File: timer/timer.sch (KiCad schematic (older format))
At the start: 29 parts, among them P1 Keypad, P2 Display, P3 Handset, P4 PWR, P5 Hook, P6 Encoder, P7 SPKR, Q1 S8050, U1 74HC595, U2 NanoEvery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

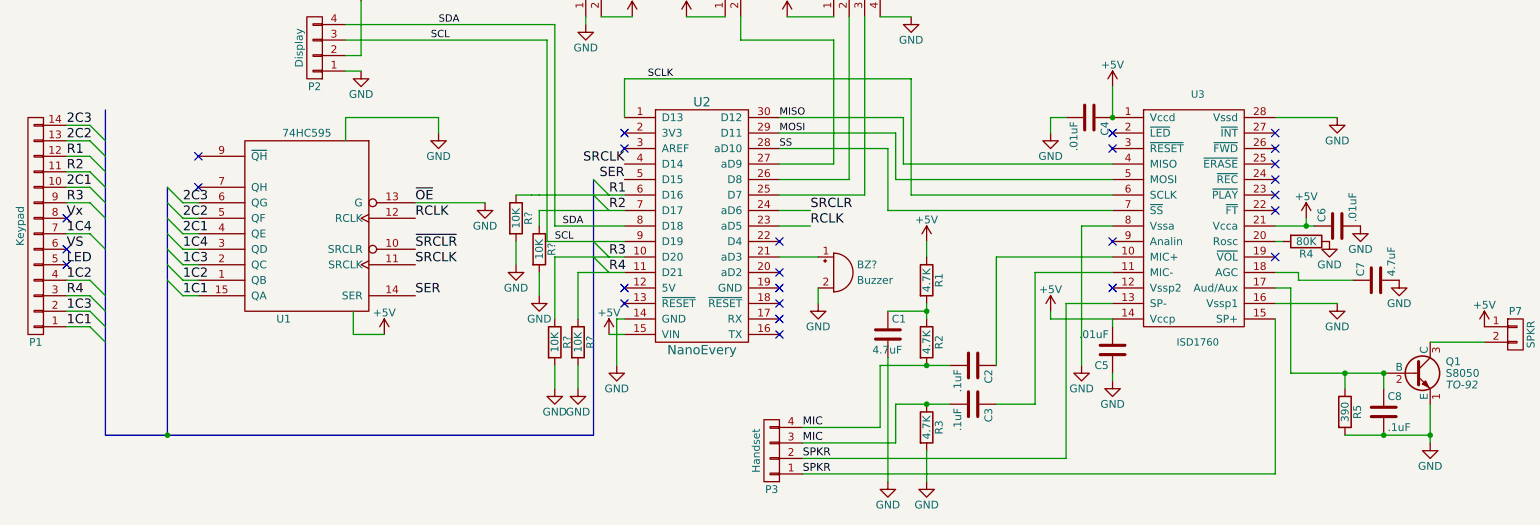
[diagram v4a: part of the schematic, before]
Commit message: More moved buzzer t d2
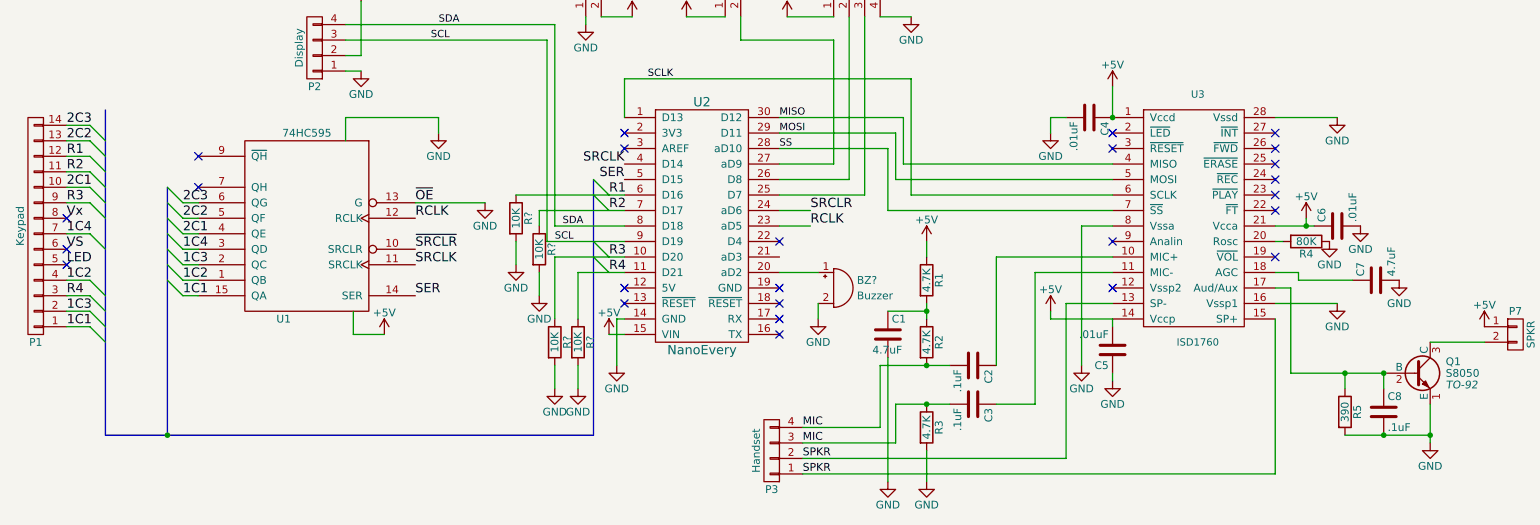
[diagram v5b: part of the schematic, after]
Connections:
- net at U2.20 (aD2): now also BZ?.1 (-)
- net at U2.21 (aD3): no longer BZ?.1 (-)
- no-connect marks 26 -> 25
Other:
- moved on the sheet: BZ?
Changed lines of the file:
@@
 	3050 2400 3050 2050
 Wire Wire Line
-	4250 3600 4550 3600
-Wire Wire Line
-	4550 3600 4750 3600
+	4250 3600 4750 3600
 Wire Wire Line
 	4250 3600 4250 2300
@@
 	7500 2800 7500 2900
 Wire Wire Line
-	8950 3500 9150 3500
-Wire Wire Line
-	9150 3500 9200 3500
+	8950 3500 9200 3500
 Wire Wire Line
 	8950 3800 9100 3800
@@
 	7150 3700 7900 3700
 Wire Wire Line
-	6700 4000 6700 4050
-Wire Wire Line
-	6700 4050 6700 4100
+	6700 4000 6700 4100
 Wire Wire Line
 	6700 4950 6700 5150
@@
 	6400 4800 6400 4400
 Wire Wire Line
-	6400 4400 6700 4400
-Wire Wire Line
-	6700 4400 6850 4400
+	6400 4400 6850 4400
 Wire Wire Line
 	5900 4900 6500 4900
@@
 	6500 4900 6500 4650
 Wire Wire Line
-	6500 4650 6700 4650
-Wire Wire Line
-	6700 4650 6850 4650
+	6500 4650 6850 4650
 Connection ~ 6700 4650
 Connection ~ 6700 4050
@@
 	9050 3900 9050 4450
 Wire Wire Line
-	9050 4450 9400 4450
-Wire Wire Line
-	9400 4450 9650 4450
+	9050 4450 9650 4450
 Connection ~ 9400 4450
 Connection ~ 9650 4450
@@
 	9650 4450 9650 4550
 Wire Wire Line
-	9400 4850 9650 4850
-Wire Wire Line
-	9650 4850 9950 4850
-Wire Wire Line
-	9950 4650 9950 4850
-Wire Wire Line
-	9950 4850 9950 4900
+	9400 4850 9950 4850
+Wire Wire Line
+	9950 4650 9950 4900
 Connection ~ 9950 4850
 Connection ~ 9650 4850
@@
 	3400 3350 3850 3350
 Wire Bus Line
-	1400 2750 1400 2950
+	1400 2750 1400 4850
 Wire Bus Line
-	1400 2950 1400 3050
-Wire Bus Line
-	1400 3050 1400 3150
-Wire Bus Line
-	1400 3150 1400 3250
-Wire Bus Line
-	1400 3250 1400 3350
-Wire Bus Line
-	1400 3350 1400 3450
-Wire Bus Line
-	1400 3450 1400 3650
-Wire Bus Line
-	1400 3650 1400 3950
-Wire Bus Line
-	1400 3950 1400 4050
-Wire Bus Line
-	1400 4050 1400 4150
-Wire Bus Line
-	1400 4150 1400 4250
-Wire Bus Line
-	1400 4250 1400 4850
-Wire Bus Line
-	4550 4850 4550 3700
-Wire Bus Line
-	4550 3700 4550 3600
-Wire Bus Line
-	4550 3600 4550 3300
-Wire Bus Line
-	4550 3300 4550 3200
+	4550 4850 4550 3200
 Entry Wire Line
 	1300 2850 1400 2950
@@
 Connection ~ 1800 4850
 Wire Bus Line
-	1800 3250 1800 3350
-Wire Bus Line
-	1800 3350 1800 3450
-Wire Bus Line
-	1800 3450 1800 3550
-Wire Bus Line
-	1800 3550 1800 3650
-Wire Bus Line
-	1800 3650 1800 3750
-Wire Bus Line
-	1800 3750 1800 3850
-Wire Bus Line
-	1800 3850 1800 4850
+	1800 3250 1800 4850
 Entry Wire Line
 	1800 3850 1900 3950
@@
 	4550 3700 4650 3800
 Wire Wire Line
-	4200 3300 4550 3300
-Wire Wire Line
-	4550 3300 4650 3300
-Wire Wire Line
-	4650 3300 4750 3300
-Wire Wire Line
-	4500 3400 4650 3400
-Wire Wire Line
-	4650 3400 4750 3400
-Wire Wire Line
-	4300 3700 4550 3700
-Wire Wire Line
-	4550 3700 4650 3700
-Wire Wire Line
-	4650 3700 4750 3700
-Wire Wire Line
-	4450 3800 4650 3800
-Wire Wire Line
-	4650 3800 4750 3800
+	4050 3300 4750 3300
+Wire Wire Line
+	4200 3400 4750 3400
+Wire Wire Line
+	4300 3700 4750 3700
+Wire Wire Line
+	4450 3800 4750 3800
 Text Label 4650 3300 0    60   ~ 0
 R1
@@
 RCLK
 Wire Bus Line
-	1400 4850 1800 4850
-Wire Bus Line
-	1800 4850 4550 4850
+	1400 4850 4550 4850
 Entry Wire Line
 	4550 3200 4650 3300
@@
 NoConn ~ 5750 4000
 NoConn ~ 5750 3900
-NoConn ~ 5750 3800
 NoConn ~ 5750 3600
 NoConn ~ 4750 3000
@@
 L Buzzer BZ?
 U 1 1 5E27DCA2
-P 6100 3800
-F 0 "BZ?" H 6250 3850 50  0000 L CNN
-F 1 "Buzzer" H 6250 3750 50  0000 L CNN
-F 2 "" V 6075 3900 50  0000 C CNN
-F 3 "" V 6075 3900 50  0000 C CNN
-	1    6100 3800
-	1    0    0    -1
-$EndComp
-Wire Wire Line
-	5750 3700 6000 3700
+P 6100 3900
+F 0 "BZ?" H 6250 3950 50  0000 L CNN
+F 1 "Buzzer" H 6250 3850 50  0000 L CNN
+F 2 "" V 6075 4000 50  0000 C CNN
+F 3 "" V 6075 4000 50  0000 C CNN
+	1    6100 3900
+	1    0    0    -1
+$EndComp
 $Comp
 L GND #PWR?
 U 1 1 5E27DE4E
-P 6000 4000
-F 0 "#PWR?" H 6000 3750 50  0001 C CNN
-F 1 "GND" H 6000 3850 50  0000 C CNN
-F 2 "" H 6000 4000 50  0000 C CNN
-F 3 "" H 6000 4000 50  0000 C CNN
-	1    6000 4000
-	1    0    0    -1
-$EndComp
-Wire Wire Line
-	6000 3900 6000 4000
+P 6000 4100
+F 0 "#PWR?" H 6000 3850 50  0001 C CNN
+F 1 "GND" H 6000 3950 50  0000 C CNN
+F 2 "" H 6000 4100 50  0000 C CNN
+F 3 "" H 6000 4100 50  0000 C CNN
+	1    6000 4100
+	1    0    0    -1
+$EndComp
+Wire Wire Line
+	6000 4000 6000 4100
 $Comp
 L R R?
@@
 	4300 3700 4300 4100
 Wire Wire Line
-	4500 3400 4200 3400
-Wire Wire Line
 	4200 3400 4200 3500
-Wire Wire Line
-	4200 3300 4200 3300
-Wire Wire Line
-	4200 3300 4150 3300
-Wire Wire Line
-	4150 3300 4050 3300
 $Comp
 L GND #PWR?
@@
 Wire Wire Line
 	4450 4400 4450 4550
+Wire Wire Line
+	5750 3800 6000 3800
 $EndSCHEMATC

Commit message: Schematic update (traistor for buzzer)
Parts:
- added Q2: PN2222A, symbol PN2222A
- added R10: 100, symbol R
- gave numbers to parts that had none: 5
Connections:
- net SRCLR is gone; now on net ~SRCLR: U2.24 (aD6)
- net +5V: now also R10.1
- net GND: now also Q2.1 (E); no longer BZ1.2 (+)
- net at U2.20 (aD2): now also Q2.2 (B); no longer BZ1.1 (-)
- net MIC renamed MIC+
- net SPKR renamed SPKR+
- net SPKR+: no longer P3.2 (P2), U3.13 (SP-)
- new net: BZ1.1 (-), R10.2
- new net: BZ1.2 (+), Q2.3 (C)
- new net SPKR-: P3.2 (P2), U3.13 (SP-)
- no-connect marks 25 -> 26
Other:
- moved on the sheet: BZ1, C2, C3, P3, R1, R2, R3
